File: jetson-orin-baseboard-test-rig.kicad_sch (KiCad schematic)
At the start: 79 parts, among them J1 PinHeader_2x6_P2.54mm_Drill1.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, J10 Harwin_1x1_H17.75mm_Drill0.8m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, J11 Harwin_1x1_H17.75mm_Drill0.8m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, J12 Harwin_1x1_H17.75mm_Drill0.8m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, J13 Harwin_1x1_H17.75mm_Drill0.8m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, J14 Harwin_1x1_H17.75mm_Drill0.8m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, J15 Harwin_1x1_H17.75mm_Drill0.8m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, J16 Harwin_1x1_H17.75mm_Drill0.8m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, J17 Harwin_1x1_H17.75mm_Drill0.8m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, J18 Harwin_1x1_H17.75mm_Drill0.8m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, J19 Harwin_1x1_H17.75mm_Drill0.8m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, J2 PinHeader_2x6_P2.54mm_Drill1.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, J20 Harwin_1x1_H17.75mm_Drill0.8m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, J21 Harwin_1x1_H17.75mm_Drill0.8m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, J22 Harwin_1x1_H17.75mm_Drill0.8m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, J23 Harwin_1x1_H17.75mm_Drill0.8m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, J24 Harwin_1x1_H17.75mm_Drill0.8m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, J25 Harwin_1x1_H17.75mm_Drill0.8m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, J26 Harwin_1x1_H17.75mm_Drill0.8m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, J27 Harwin_1x1_H17.75mm_Drill0.8m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, J28 Harwin_1x1_H17.75mm_Drill0.8m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, J29 Harwin_1x1_H17.75mm_Drill0.8m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, J3 PinHeader_2x6_P2.54mm_Drill1.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, J30 Harwin_1x1_H17.75mm_Drill0.8m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, J4 PinHeader_2x6_P2.54mm_Drill1.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, J5 PinHeader_2x6_P2.54mm_Drill1.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, J6 PinHeader_2x6_P2.54mm_Drill1.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, J7 PinHeader_2x6_P2.54mm_Drill1.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, J8 Harwin_1x1_H17.75mm_Drill0.8m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, J9 Harwin_1x1_H17.75mm_Drill0.8m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, Q1 BSS84

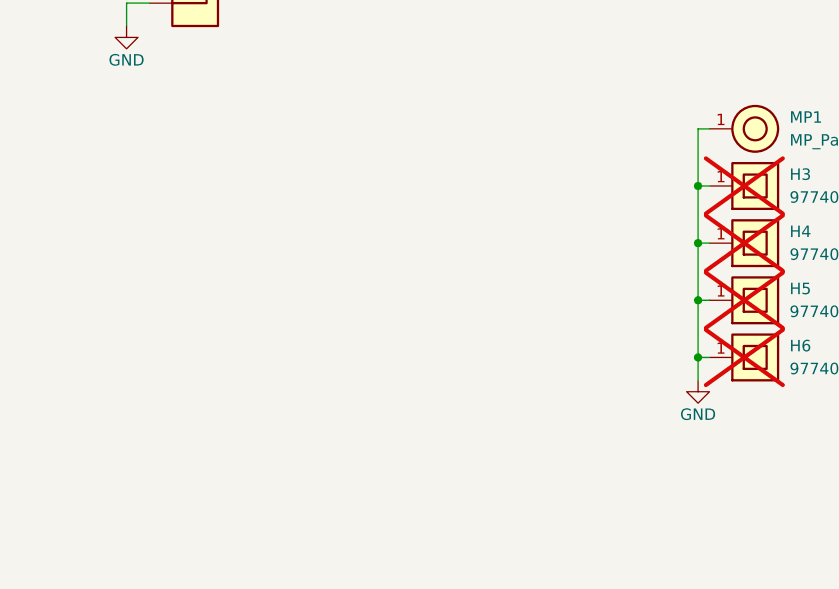
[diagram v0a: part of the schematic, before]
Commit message: [77400] Add studs
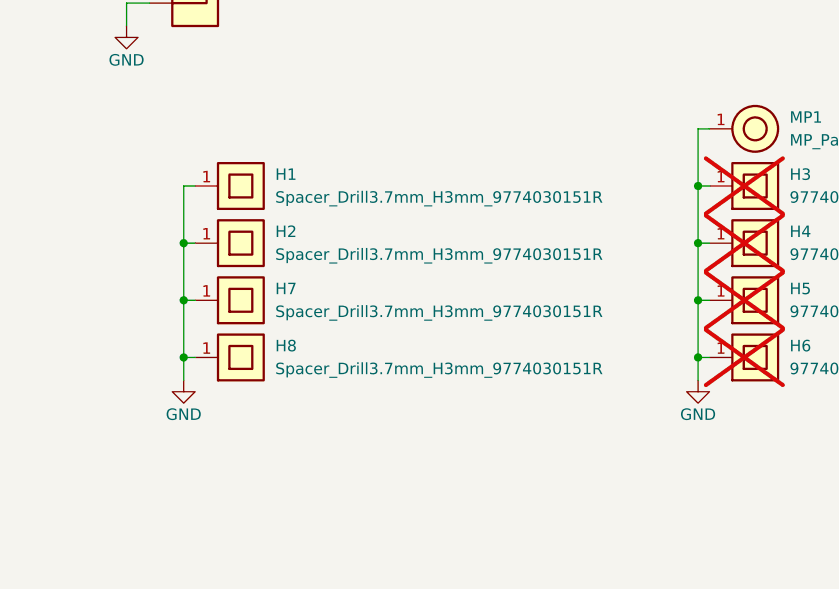
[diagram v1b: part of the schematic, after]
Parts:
- added H1, H2, H7, H8: Spacer_Drill3.7mm_H3mm_9774030151R, antmicro-footprints:Spacer_Drill3.7mm_H3mm_9774030151R, symbol antmicroMechanicalParts:Spacer_Drill3.7mm_H3mm_9774030151R
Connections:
- net GND: now also H1.1, H2.1, H7.1, H8.1

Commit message: [#77400] Update mounting studs
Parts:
- removed H1, H2, H7, H8: Spacer_Drill3.7mm_H3mm_9774030151R, antmicro-footprints:Spacer_Drill3.7mm_H3mm_9774030151R, symbol antmicroMechanicalParts:Spacer_Drill3.7mm_H3mm_9774030151R
- added H1, H2, H7, H8: Spacer_Drill3.7mm_H5mm_9774050151R, antmicro-footprints:Spacer_Drill3.7mm_H5mm_9774050151R, symbol antmicroMechanicalParts:Spacer_Drill3.7mm_H5mm_9774050151R
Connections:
- net GND: now also H1.1, H2.1, H7.1, H8.1
